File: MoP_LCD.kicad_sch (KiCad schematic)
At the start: 6 parts, among them J20 Conn_01x16

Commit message: Finished schematics
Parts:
- C1001: renamed from C11; footprint (none) -> Capacitor_SMD:C_0805_2012Metric_Pad1.18x1.45mm_HandSolder
- J1001: renamed from J20; footprint (none) -> Connector_PinHeader_1.00mm:PinHeader_1x16_P1.00mm_Vertical
- JP7: footprint (none) -> Connector_PinHeader_2.54mm:PinHeader_1x02_P2.54mm_Vertical
- R1001: renamed from R49; footprint (none) -> Resistor_SMD:R_0805_2012Metric
- R1002: renamed from R20; footprint (none) -> Resistor_SMD:R_0805_2012Metric
- renumbered RV1 to P1001
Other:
- moved on the sheet: C1001, R1002
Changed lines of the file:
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@@
 	(wire
 		(pts
-			(xy 160.02 74.93) (xy 160.02 78.74)
+			(xy 160.02 74.93) (xy 160.02 77.47)
 		)
 		(stroke
@@
 	(wire
 		(pts
-			(xy 149.86 86.36) (xy 149.86 115.57)
+			(xy 149.86 85.09) (xy 149.86 115.57)
 		)
 		(stroke
@@
 	(wire
 		(pts
-			(xy 160.02 86.36) (xy 160.02 115.57)
+			(xy 160.02 85.09) (xy 160.02 115.57)
 		)
 		(stroke
@@
 	(wire
 		(pts
-			(xy 149.86 74.93) (xy 149.86 78.74)
+			(xy 149.86 74.93) (xy 149.86 77.47)
 		)
 		(stroke
@@
 		(on_board yes)
 		(dnp no)
-		(property "Reference" "R49"
+		(property "Reference" "R1001"
 			(at 123.19 77.216 90)
 			(effects
@@
 			)
 		)
-		(property "Footprint" ""
+		(property "Footprint" "Resistor_SMD:R_0805_2012Metric"
 			(at 123.19 81.788 90)
 			(effects
@@
 			(project "MoP"
 				(path "/4d76798e-9a11-4d8d-a723-72f274a89091/d35d25c1-d5ff-4296-8cd7-8485bcc0a02c"
-					(reference "R49")
+					(reference "R1001")
 					(unit 1)
 				)
@@
 		(dnp no)
 		(fields_autoplaced yes)
-		(property "Reference" "J20"
-			(at 195.58 95.2499 0)
+		(property "Reference" "J1001"
+			(at 194.31 95.2499 0)
 			(effects
 				(font
@@
 		)
 		(property "Value" "Conn_01x16"
-			(at 195.58 97.7899 0)
+			(at 194.31 97.7899 0)
 			(effects
 				(font
@@
 			)
 		)
-		(property "Footprint" ""
+		(property "Footprint" "Connector_PinHeader_1.00mm:PinHeader_1x16_P1.00mm_Vertical"
 			(at 191.77 95.25 0)
 			(effects
@@
 			(project "MoP"
 				(path "/4d76798e-9a11-4d8d-a723-72f274a89091/d35d25c1-d5ff-4296-8cd7-8485bcc0a02c"
-					(reference "J20")
+					(reference "J1001")
 					(unit 1)
 				)
@@
 		(on_board yes)
 		(dnp no)
-		(fields_autoplaced yes)
-		(property "Reference" "RV1"
-			(at 166.37 81.2799 0)
+		(property "Reference" "P1001"
+			(at 177.546 78.74 0)
 			(effects
 				(font
@@
 		)
 		(property "Value" "10k"
-			(at 166.37 83.8199 0)
+			(at 174.244 84.328 0)
 			(effects
 				(font
@@
 			(project "MoP"
 				(path "/4d76798e-9a11-4d8d-a723-72f274a89091/d35d25c1-d5ff-4296-8cd7-8485bcc0a02c"
-					(reference "RV1")
+					(reference "P1001")
 					(unit 1)
 				)
@@
 	(symbol
 		(lib_id "Device:C")
-		(at 149.86 82.55 0)
+		(at 149.86 81.28 0)
 		(mirror x)
 		(unit 1)
@@
 		(on_board yes)
 		(dnp no)
-		(fields_autoplaced yes)
-		(property "Reference" "C11"
-			(at 146.05 81.2799 0)
+		(property "Reference" "C1001"
+			(at 148.844 78.232 0)
 			(effects
 				(font
@@
 		)
 		(property "Value" "C"
-			(at 146.05 83.8199 0)
+			(at 146.558 83.058 0)
 			(effects
 				(font
@@
 			)
 		)
-		(property "Footprint" ""
-			(at 150.8252 78.74 0)
+		(property "Footprint" "Capacitor_SMD:C_0805_2012Metric_Pad1.18x1.45mm_HandSolder"
+			(at 150.8252 77.47 0)
 			(effects
 				(font
@@
 		)
 		(property "Datasheet" "~"
-			(at 149.86 82.55 0)
+			(at 149.86 81.28 0)
 			(effects
 				(font
@@
 		)
 		(property "Description" "Unpolarized capacitor"
-			(at 149.86 82.55 0)
+			(at 149.86 81.28 0)
 			(effects
 				(font
@@
 			(project "MoP"
 				(path "/4d76798e-9a11-4d8d-a723-72f274a89091/d35d25c1-d5ff-4296-8cd7-8485bcc0a02c"
-					(reference "C11")
+					(reference "C1001")
 					(unit 1)
 				)
@@
 			)
 		)
-		(property "Footprint" ""
+		(property "Footprint" "Connector_PinHeader_2.54mm:PinHeader_1x02_P2.54mm_Vertical"
 			(at 123.19 74.93 0)
 			(effects
@@
 	(symbol
 		(lib_id "Device:R")
-		(at 160.02 82.55 0)
+		(at 160.02 81.28 0)
 		(mirror y)
 		(unit 1)
@@
 		(on_board yes)
 		(dnp no)
-		(property "Reference" "R20"
-			(at 157.48 81.2799 0)
+		(property "Reference" "R1002"
+			(at 158.496 78.232 0)
 			(effects
 				(font
@@
 		)
 		(property "Value" "0"
-			(at 157.48 83.8199 0)
+			(at 157.48 82.5499 0)
 			(effects
 				(font
@@
 			)
 		)
-		(property "Footprint" ""
-			(at 161.798 82.55 90)
+		(property "Footprint" "Resistor_SMD:R_0805_2012Metric"
+			(at 161.798 81.28 90)
 			(effects
 				(font
@@
 		)
 		(property "Datasheet" "~"
-			(at 160.02 82.55 0)
+			(at 160.02 81.28 0)
 			(effects
 				(font
@@
 		)
 		(property "Description" "Resistor"
-			(at 160.02 82.55 0)
+			(at 160.02 81.28 0)
 			(effects
 				(font
@@
 			(project "MoP"
 				(path "/4d76798e-9a11-4d8d-a723-72f274a89091/d35d25c1-d5ff-4296-8cd7-8485bcc0a02c"
-					(reference "R20")
+					(reference "R1002")
 					(unit 1)
 				)

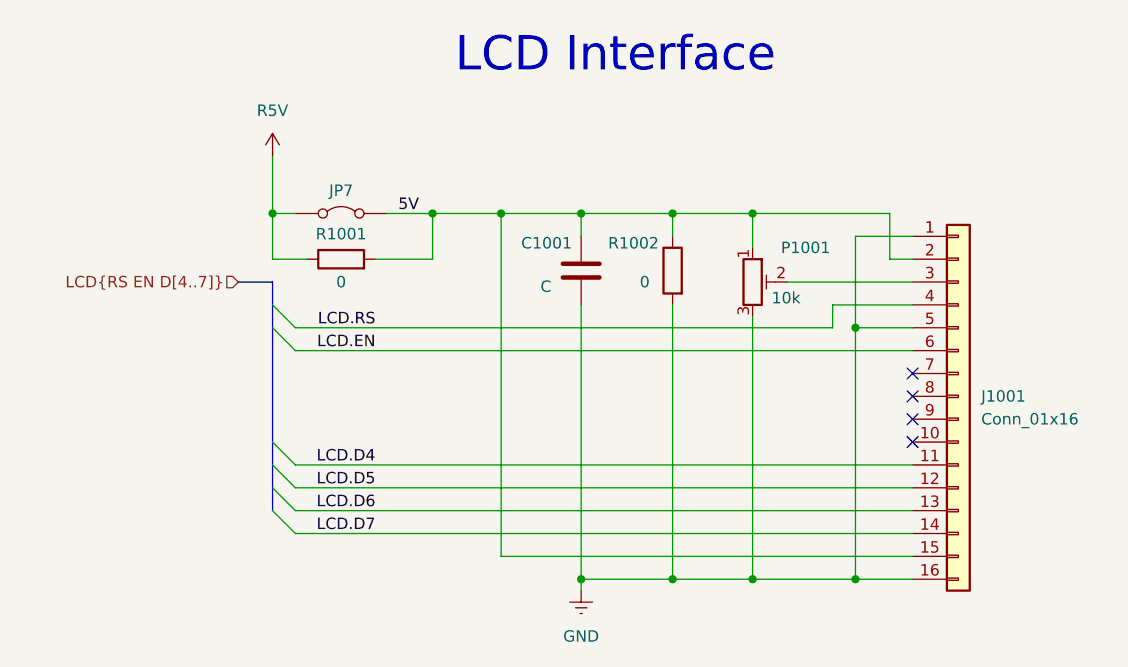
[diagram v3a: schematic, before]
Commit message: Added subproject for EPS PCB
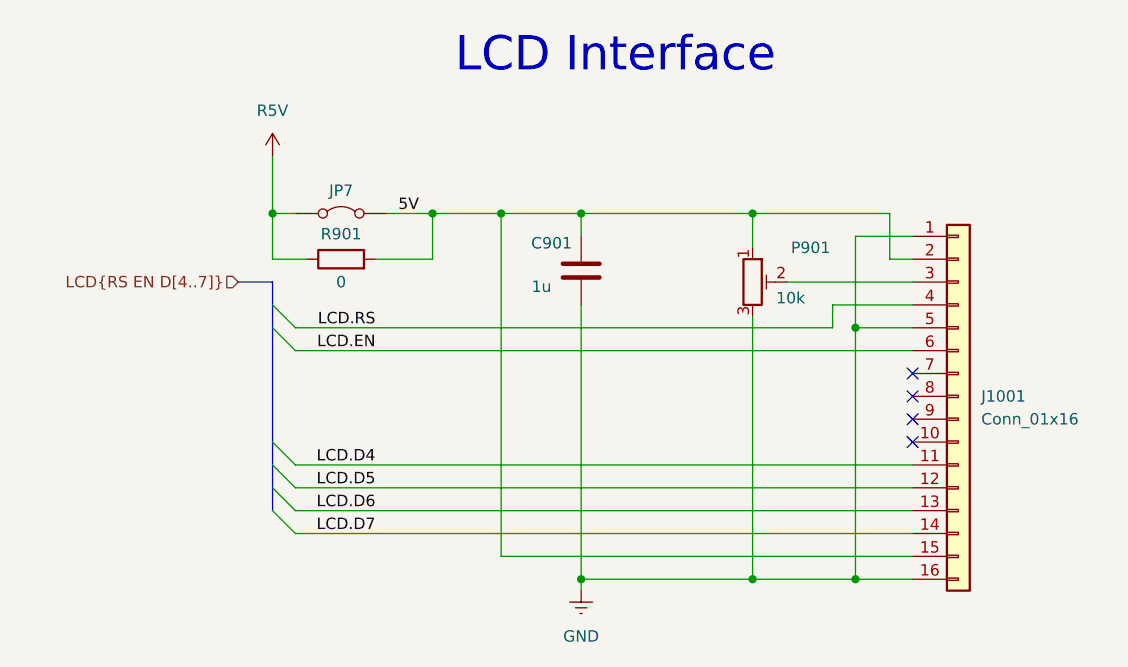
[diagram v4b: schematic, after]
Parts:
- removed R1002: 0, Resistor_SMD:R_0805_2012Metric, symbol Device:R
- C901: renamed from C1001; value C -> 1u
- P901: renamed from P1001; footprint (none) -> Connector_PinHeader_2.54mm:PinHeader_1x03_P2.54mm_Vertical
- renumbered R1001 to R901

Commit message: added OBC
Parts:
- R901: now not fitted
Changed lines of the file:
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@@
+	)
+	(symbol
+		(lib_id "power:+5V")
+		(at 115.57 68.58 0)
+		(unit 1)
+		(exclude_from_sim no)
+		(in_bom yes)
+		(on_board yes)
+		(dnp no)
+		(fields_autoplaced yes)
+		(property "Reference" "#PWR0801"
+			(at 115.57 72.39 0)
+			(effects
+				(font
+					(size 1.27 1.27)
+				)
+				(hide yes)
+			)
+		)
+		(property "Value" "R5V"
+			(at 115.57 63.5 0)
+			(effects
+				(font
+					(size 1.27 1.27)
+				)
+			)
+		)
+		(property "Footprint" ""
+			(at 115.57 68.58 0)
+			(effects
+				(font
+					(size 1.27 1.27)
+				)
+				(hide yes)
+			)
+		)
+		(property "Datasheet" ""
+			(at 115.57 68.58 0)
+			(effects
+				(font
+					(size 1.27 1.27)
+				)
+				(hide yes)
+			)
+		)
+		(property "Description" "Power symbol creates a global label with name \"+5V\""
+			(at 115.57 68.58 0)
+			(effects
+				(font
+					(size 1.27 1.27)
+				)
+				(hide yes)
+			)
+		)
+		(pin "1"
+		)
+		(instances
+			(project "OBC"
+				(path "/4fa4f4fb-851d-4975-b789-eb7f900188ea/99163bcd-f204-4e6d-aa95-ab00d27e8f54"
+					(reference "#PWR0801")
+					(unit 1)
+				)
+			)
+		)
 	)
 	(symbol
@@
 		(exclude_from_sim no)
 		(in_bom yes)
-		(on_board yes)
-		(dnp no)
+		(on_board no)
+		(dnp yes)
 		(property "Reference" "R901"
 			(at 123.19 77.216 90)
@@
 				(path "/4d76798e-9a11-4d8d-a723-72f274a89091/d35d25c1-d5ff-4296-8cd7-8485bcc0a02c"
 					(reference "R901")
+					(unit 1)
+				)
+			)
+			(project "MoP"
+				(path "/4fa4f4fb-851d-4975-b789-eb7f900188ea/99163bcd-f204-4e6d-aa95-ab00d27e8f54"
+					(reference "R801")
 					(unit 1)
 				)
@@
 				)
 			)
-		)
-	)
-	(symbol
-		(lib_id "power:+3V3")
-		(at 115.57 68.58 0)
-		(unit 1)
-		(exclude_from_sim no)
-		(in_bom yes)
-		(on_board yes)
-		(dnp no)
-		(fields_autoplaced yes)
-		(property "Reference" "#PWR031"
-			(at 115.57 72.39 0)
-			(effects
-				(font
-					(size 1.27 1.27)
-				)
-				(hide yes)
-			)
-		)
-		(property "Value" "R5V"
-			(at 115.57 63.5 0)
-			(effects
-				(font
-					(size 1.27 1.27)
-				)
-			)
-		)
-		(property "Footprint" ""
-			(at 115.57 68.58 0)
-			(effects
-				(font
-					(size 1.27 1.27)
-				)
-				(hide yes)
-			)
-		)
-		(property "Datasheet" ""
-			(at 115.57 68.58 0)
-			(effects
-				(font
-					(size 1.27 1.27)
-				)
-				(hide yes)
-			)
-		)
-		(property "Description" "Power symbol creates a global label with name \"+3V3\""
-			(at 115.57 68.58 0)
-			(effects
-				(font
-					(size 1.27 1.27)
-				)
-				(hide yes)
-			)
-		)
-		(pin "1"
-		)
-		(instances
-			(project ""
-				(path "/4d76798e-9a11-4d8d-a723-72f274a89091/d35d25c1-d5ff-4296-8cd7-8485bcc0a02c"
-					(reference "#PWR031")
+			(project "MoP"
+				(path "/4fa4f4fb-851d-4975-b789-eb7f900188ea/99163bcd-f204-4e6d-aa95-ab00d27e8f54"
+					(reference "J801")
 					(unit 1)
 				)
@@
 				(path "/4d76798e-9a11-4d8d-a723-72f274a89091/d35d25c1-d5ff-4296-8cd7-8485bcc0a02c"
 					(reference "P901")
+					(unit 1)
+				)
+			)
+			(project "MoP"
+				(path "/4fa4f4fb-851d-4975-b789-eb7f900188ea/99163bcd-f204-4e6d-aa95-ab00d27e8f54"
+					(reference "P801")
 					(unit 1)
 				)
@@
 				)
 			)
+			(project "MoP"
+				(path "/4fa4f4fb-851d-4975-b789-eb7f900188ea/99163bcd-f204-4e6d-aa95-ab00d27e8f54"
+					(reference "C801")
+					(unit 1)
+				)
+			)
 		)
 	)
@@
 				)
 			)
+			(project "MoP"
+				(path "/4fa4f4fb-851d-4975-b789-eb7f900188ea/99163bcd-f204-4e6d-aa95-ab00d27e8f54"
+					(reference "JP801")
+					(unit 1)
+				)
+			)
 		)
 	)
@@
 					(reference "#PWR011")
 					(unit 1)
+				)
+			)
+			(project ""
+				(path "/4fa4f4fb-851d-4975-b789-eb7f900188ea/99163bcd-f204-4e6d-aa95-ab00d27e8f54"
+					(reference "#PWR011")
+					(unit 1)
